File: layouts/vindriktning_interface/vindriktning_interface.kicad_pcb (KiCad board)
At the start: 2 copper layers, 8 parts

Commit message: Migrate layout partially
omit routing and zones amongst others
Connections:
- D1 pad 2: fan_controller-gnd-1 -> fan_controller-gnd
- FanConnector1 pad 1: fan_controller-gnd-1 -> fan_controller-gnd
- J1 pad 1: line -> line-2
- J1 pad 2: line-2 -> line-4
- Q1 pad 1: line-1 -> line-3
- Q1 pad 2: fan_controller-gnd-1 -> fan_controller-gnd
- Q1 pad 3: fan_controller-gnd -> fan_controller-gnd-1
- R1 pad 1: line-1 -> line-3
- R2 pad 2: fan_controller-gnd-1 -> fan_controller-gnd
- U1 pad 1: line-2 -> line-4
- U1 pad 4: line-3 -> line-1
- U1 pad 5: line-4 -> line
- U1 pad 8: line -> line-2
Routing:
- net fan_controller-gnd-1: track 6.53 -> 0.00 mm
- net fan_controller-gnd: track 0.00 -> 6.53 mm
- net line-3: track 0.00 -> 1.55 mm
- net line-1: track 1.55 -> 0.00 mm
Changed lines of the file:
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@@
     (net 1 "cathode")
     (net 2 "hv-1")
-    (net 3 "line")
+    (net 3 "line-2")
     (net 4 "fan_controller.fan_connector.footprint.pins[3].net-net")
-    (net 5 "line-1")
+    (net 5 "line-3")
     (net 6 "fan_controller-hv")
     (net 7 "fan_controller.fan_connector.footprint.pins[2].net-net")
@@
     (net 9 "hv")
     (net 10 "gnd")
-    (net 11 "fan_controller-gnd")
+    (net 11 "fan_controller-gnd-1")
     (net 12 "gnd-1")
-    (net 13 "line-4")
-    (net 14 "line-3")
+    (net 13 "line")
+    (net 14 "line-1")
     (net 15 "mount[0]")
-    (net 16 "fan_controller-gnd-1")
-    (net 17 "line-2")
+    (net 16 "fan_controller-gnd")
+    (net 17 "line-4")
     (footprint "atopile:R0603-ebcab9"
         (layer "F.Cu")
@@
             (layers "F.Cu" "F.Paste" "F.Mask")
             (remove_unused_layers no)
-            (net 5 "line-1"))
+            (net 5 "line-3"))
         (pad "2" smd rect
             (at 0.75 0 180)
@@
             (layers "F.Cu" "F.Paste" "F.Mask")
             (remove_unused_layers no)
-            (net 16 "fan_controller-gnd-1"))
+            (net 16 "fan_controller-gnd"))
         (pad "2" smd rect
             (at 0.63 -1.45 90)
@@
             (layers "F.Cu" "F.Paste" "F.Mask")
             (remove_unused_layers no)
-            (net 17 "line-2"))
+            (net 17 "line-4"))
         (pad "2" smd rect
             (at -0.25 1.55 180)
@@
             (layers "F.Cu" "F.Paste" "F.Mask")
             (remove_unused_layers no)
-            (net 14 "line-3"))
+            (net 14 "line-1"))
         (pad "5" smd rect
             (at 0.76 -1.55 180)
@@
             (layers "F.Cu" "F.Paste" "F.Mask")
             (remove_unused_layers no)
-            (net 13 "line-4"))
+            (net 13 "line"))
         (pad "6" smd rect
             (at 0.25 -1.55 180)
@@
             (layers "F.Cu" "F.Paste" "F.Mask")
             (remove_unused_layers no)
-            (net 3 "line")))
+            (net 3 "line-2")))
     (footprint "atopile:SOT-23-3_L2.9-W1.3-P1.90-LS2.4-BL-1-fcaf94"
         (layer "F.Cu")
@@
             (layers "F.Cu" "F.Paste" "F.Mask")
             (remove_unused_layers no)
-            (net 5 "line-1"))
+            (net 5 "line-3"))
         (pad "2" smd rect
             (at 0.95 1 0)
@@
             (layers "F.Cu" "F.Paste" "F.Mask")
             (remove_unused_layers no)
-            (net 16 "fan_controller-gnd-1"))
+            (net 16 "fan_controller-gnd"))
         (pad "3" smd rect
             (at 0 -1 0)
@@
             (layers "F.Cu" "F.Paste" "F.Mask")
             (remove_unused_layers no)
-            (net 11 "fan_controller-gnd")))
+            (net 11 "fan_controller-gnd-1")))
     (footprint "atopile:SOD-323_L1.8-W1.3-LS2.5-RD-b55baa"
         (layer "F.Cu")
@@
             (layers "F.Cu" "F.Paste" "F.Mask")
             (remove_unused_layers no)
-            (net 16 "fan_controller-gnd-1")))
+            (net 16 "fan_controller-gnd")))
     (footprint "atopile:CONN-SMD_ZH1.5-4AB-9aedad"
         (layer "F.Cu")
@@
             (layers "F.Cu" "F.Paste" "F.Mask")
             (remove_unused_layers no)
-            (net 3 "line"))
+            (net 3 "line-2"))
         (pad "2" smd rect
             (at -0.75 1.12 0)
@@
             (layers "F.Cu" "F.Paste" "F.Mask")
             (remove_unused_layers no)
-            (net 17 "line-2"))
+            (net 17 "line-4"))
         (pad "3" smd rect
             (at 0.75 1.12 0)
@@
             (layers "F.Cu" "F.Paste" "F.Mask")
             (remove_unused_layers no)
-            (net 16 "fan_controller-gnd-1")))
+            (net 16 "fan_controller-gnd")))
     (segment
         (start 10.75 -10.25)

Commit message: Regenerate layouts
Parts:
- moved U1 14.7 mm to (9.00, -13.5), turned to 90 degrees
- moved J1 13.4 mm to (10.0, -18.1)
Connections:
- J1 pad 1: line-2 -> line
- J1 pad 2: line-4 -> line-2
- J1 pad 3: hv -> hv-1
- J1 pad 4: gnd -> gnd-1
- Q1 pad 1: line-3 -> line-1
- R1 pad 1: line-3 -> line-1
- R1 pad 2: gnd-1 -> gnd
- U1 pad 1: line-4 -> line-2
- U1 pad 2: gnd -> gnd-1
- U1 pad 3: hv-1 -> hv
- U1 pad 4: line-1 -> line-4
- U1 pad 5: line -> line-3
- U1 pad 6: hv-1 -> hv
- U1 pad 7: hv -> hv-1
- U1 pad 8: line-2 -> line
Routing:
- net hv-1: track 0.00 -> 12.3 mm
- net line: track 0.00 -> 5.70 mm
- net line-2: track 0.00 -> 5.22 mm
- net hv: track 0.00 -> 3.14 mm, vias 0 -> 2
- net line-3: track 1.55 -> 0.00 mm
- net line-1: track 0.00 -> 1.55 mm

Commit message: Update layouts
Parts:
- D2: value infV -> (none)
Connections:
- J1 pad 1: line -> line-1
- J1 pad 4: gnd-1 -> gnd
- Q1 pad 1: line-1 -> line-3
- R1 pad 1: line-1 -> line-3
- R1 pad 2: gnd -> gnd-1
- U1 pad 2: gnd-1 -> gnd
- U1 pad 5: line-3 -> line
- U1 pad 8: line -> line-1
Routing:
- net line: track 5.70 -> 0.00 mm
- net line-1: track 1.55 -> 5.70 mm
- net line-3: track 0.00 -> 1.55 mm
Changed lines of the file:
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@@
     (net 1 "cathode")
     (net 2 "hv")
-    (net 3 "line")
+    (net 3 "line-1")
     (net 4 "fan_controller.fan_connector.footprint.pins[3].net-net")
-    (net 5 "line-1")
+    (net 5 "line-3")
     (net 6 "fan_controller-hv")
     (net 7 "fan_controller.fan_connector.footprint.pins[2].net-net")
     (net 8 "mount[1]")
     (net 9 "hv-1")
-    (net 10 "gnd-1")
+    (net 10 "gnd")
     (net 11 "fan_controller-gnd-1")
-    (net 12 "gnd")
-    (net 13 "line-3")
+    (net 12 "gnd-1")
+    (net 13 "line")
     (net 14 "line-4")
     (net 15 "mount[0]")
@@
             (layers "F.Cu" "F.Paste" "F.Mask")
             (remove_unused_layers no)
-            (net 5 "line-1"))
+            (net 5 "line-3"))
         (pad "2" smd rect
             (at 0.75 0 180)
@@
             (layers "F.Cu" "F.Paste" "F.Mask")
             (remove_unused_layers no)
-            (net 12 "gnd")))
+            (net 12 "gnd-1")))
     (footprint "atopile:CONN-SMD_1.25-2P-ea2134"
         (layer "F.Cu")
@@
             (layers "F.Cu" "F.Paste" "F.Mask")
             (remove_unused_layers no)
-            (net 10 "gnd-1"))
+            (net 10 "gnd"))
         (pad "3" smd rect
             (at 0.25 1.55 270)
@@
             (layers "F.Cu" "F.Paste" "F.Mask")
             (remove_unused_layers no)
-            (net 13 "line-3"))
+            (net 13 "line"))
         (pad "6" smd rect
             (at 0.25 -1.55 270)
@@
             (layers "F.Cu" "F.Paste" "F.Mask")
             (remove_unused_layers no)
-            (net 3 "line")))
+            (net 3 "line-1")))
     (footprint "atopile:SOT-23-3_L2.9-W1.3-P1.90-LS2.4-BL-1-fcaf94"
         (layer "F.Cu")
@@
             (layers "F.Cu" "F.Paste" "F.Mask")
             (remove_unused_layers no)
-            (net 5 "line-1"))
+            (net 5 "line-3"))
         (pad "2" smd rect
             (at 0.95 1 0)
@@
             (layers "F.Cu" "F.Paste" "F.Mask")
             (remove_unused_layers no)
-            (net 3 "line"))
+            (net 3 "line-1"))
         (pad "2" smd rect
             (at -0.75 1.12 0)
@@
             (layers "F.Cu" "F.Paste" "F.Mask")
             (remove_unused_layers no)
-            (net 10 "gnd-1"))
+            (net 10 "gnd"))
         (pad "5" smd rect
             (at -4.5 -1.12 0)
@@
                     (size 1 1)
                     (thickness 0.15))))
-        (property "Value" "infV"
+        (property "Value" ""
             (at 0 4 -90)
             (layer "F.Fab")

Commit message: Update layout
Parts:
- moved J1 18.9 mm to (11.1, 0.80), turned to 180 degrees
- moved D1 11.2 mm to (0.00, -3.50)
- moved D2 11.2 mm to (3.25, -3.25)
- moved FanConnector1 11.2 mm to (0.00, 0.00)
- moved Q1 11.2 mm to (-4.00, -4.50)
- moved R1 11.2 mm to (-3.75, -2.00)
- moved R2 11.2 mm to (0.00, -5.25)
- moved U1 10.6 mm to (6.50, -3.25), turned to 0 degrees
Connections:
- J1 pad 1: line-1 -> line
- J1 pad 2: line-2 -> line-1
- J1 pad 4: gnd -> gnd-1
- Q1 pad 1: line-3 -> line-4
- R1 pad 1: line-3 -> line-4
- R1 pad 2: gnd-1 -> gnd
- U1 pad 1: line-2 -> line-1
- U1 pad 2: gnd -> gnd-1
- U1 pad 4: line-4 -> line-3
- U1 pad 5: line -> line-2
- U1 pad 8: line-1 -> line
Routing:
- net line: track 0.00 -> 11.1 mm
- net line-2: track 5.22 -> 0.00 mm
- net line-1: track 5.70 -> 9.35 mm
- net hv-1: track 12.3 -> 15.7 mm, vias 0 -> 2
- net line-4: track 0.00 -> 1.55 mm
- net line-3: track 1.55 -> 1.20 mm, vias 0 -> 1

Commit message: do some layouts
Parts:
- removed D1: 450mV, atopile:SOD-323_L1.8-W1.3-LS2.5-RD-b55baa
- removed D2: , atopile:LED0805-R-RD-d1137b
- removed FanConnector1: , atopile:CONN-SMD_1.25-2P-ea2134
- removed J1: , atopile:CONN-SMD_ZH1.5-4AB-9aedad
- removed Q1: , atopile:SOT-23-3_L2.9-W1.3-P1.90-LS2.4-BL-1-fcaf94
- added C1: 100nF ±10% 50V X7R, atopile:C0603-bd72f6, F.Cu at (0.17, 11.2)
- added C2: 1µF ±10% 50V X5R, atopile:C0603-bd72f6, F.Cu at (-2.40, 8.30)
- added C3: 20pF ±5% 50V C0G, atopile:C0402-b3ef17, F.Cu at (8.54, 4.34)
- added C4: 20pF ±5% 50V C0G, atopile:C0402-b3ef17, F.Cu at (8.54, 6.64)
- added C5: 100nF ±10% 50V X7R, atopile:C0603-bd72f6, F.Cu at (-1.42, 11.2)
- added R3: 0Ω 100mW, atopile:R0603-ebcab9, F.Cu at (7.20, 2.50)
- added R4: 10kΩ ±1% 100mW, atopile:R0603-ebcab9, F.Cu at (-0.75, 8.20)
- added R5: 10kΩ ±1% 100mW, atopile:R0603-ebcab9, F.Cu at (6.60, -2.40)
- added R6: 10kΩ ±1% 100mW, atopile:R0603-ebcab9, F.Cu at (-3.00, 11.2)
- added S1: , atopile:KEY-SMD_4P-L4.2-W3.2-P2.20-LS4.6-a2ccf0, F.Cu at (4.17, 9.60)
- added S2: , atopile:KEY-SMD_4P-L4.2-W3.2-P2.20-LS4.6-a2ccf0, F.Cu at (-5.43, 9.60)
- added XTAL1: , atopile:CRYSTAL-SMD_L3.2-W1.5-1-214bf9, F.Cu at (6.90, 5.20)
- U1: footprint atopile:VSON8_L2.0-W2.3-P0.50-LS3.1-BL-9e6526 -> atopile:WIFIM-SMD_ESP32-C3-MINI-MINI-1U-1cb675
- moved R1 14.3 mm to (1.75, 11.2), turned to 90 degrees
- moved R2 13.5 mm to (1.60, 8.20), turned to -90 degrees
- moved U1 7.27 mm to (0.00, 0.00), turned to 90 degrees
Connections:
- net line-3 renamed mcu.esp32_c3_mini_1.ic.footprint.pins[33].net-net
- R1 pad 1: line-4 -> mcu.boot_switch-line
- R1 pad 2: gnd -> mcu-line
- R2 pad 1: cathode -> mcu-line
- R2 pad 2: fan_controller-gnd -> hv
- U1 pad 1: line-1 -> gnd
- U1 pad 2: gnd-1 -> gnd
- U1 pad 5: line-2 -> mcu-line-1
- U1 pad 6: hv -> mcu.esp32_c3_mini_1.ic-line
- U1 pad 7: hv-1 -> mcu.esp32_c3_mini_1.ic.footprint.pins[58].net-net
- U1 pad 8: line -> mcu-line
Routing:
- net mcu-line-2: track 0.00 -> 22.1 mm, vias 0 -> 2
- net hv-1: track 15.7 -> 0.00 mm, vias 2 -> 0
- net line: track 11.1 -> 0.00 mm
- net line-1: track 9.35 -> 0.00 mm
- net mcu-line: track 0.00 -> 7.37 mm
- net fan_controller-gnd: track 6.53 -> 0.00 mm
- net mcu.reset_switch-line: track 0.00 -> 5.64 mm
- net mcu.boot_switch-line: track 0.00 -> 5.63 mm
- net fan_controller-hv: track 5.20 -> 0.00 mm
- net mcu-line-7: track 0.00 -> 4.79 mm
- net hv: track 3.14 -> 7.66 mm, vias 2 -> 3
- net unnamed[0]: track 0.00 -> 3.84 mm
- net cathode: track 2.89 -> 0.00 mm
- net mcu-line-4: track 0.00 -> 2.21 mm
- net mcu-line-9: track 0.00 -> 1.67 mm
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- added copper zone on F.Cu, net gnd

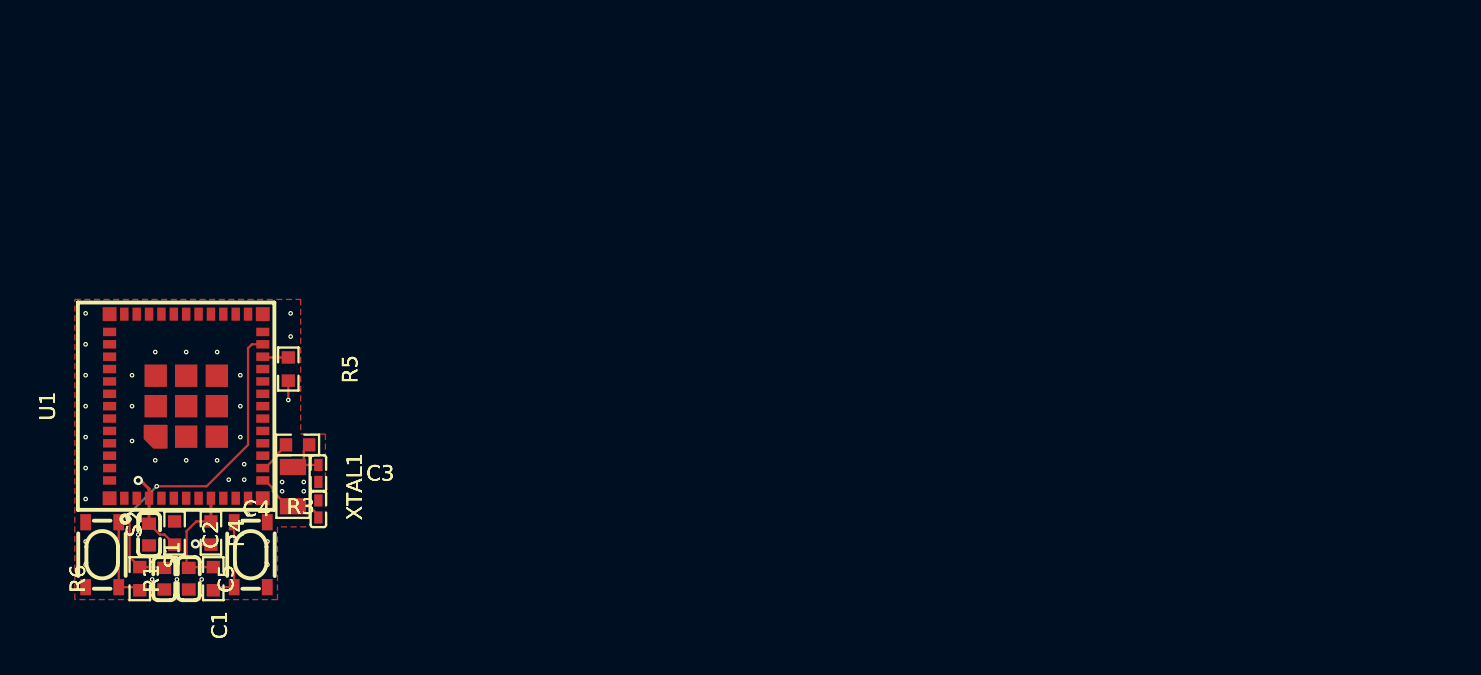
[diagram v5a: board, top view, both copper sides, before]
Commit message: Try to fix fuses
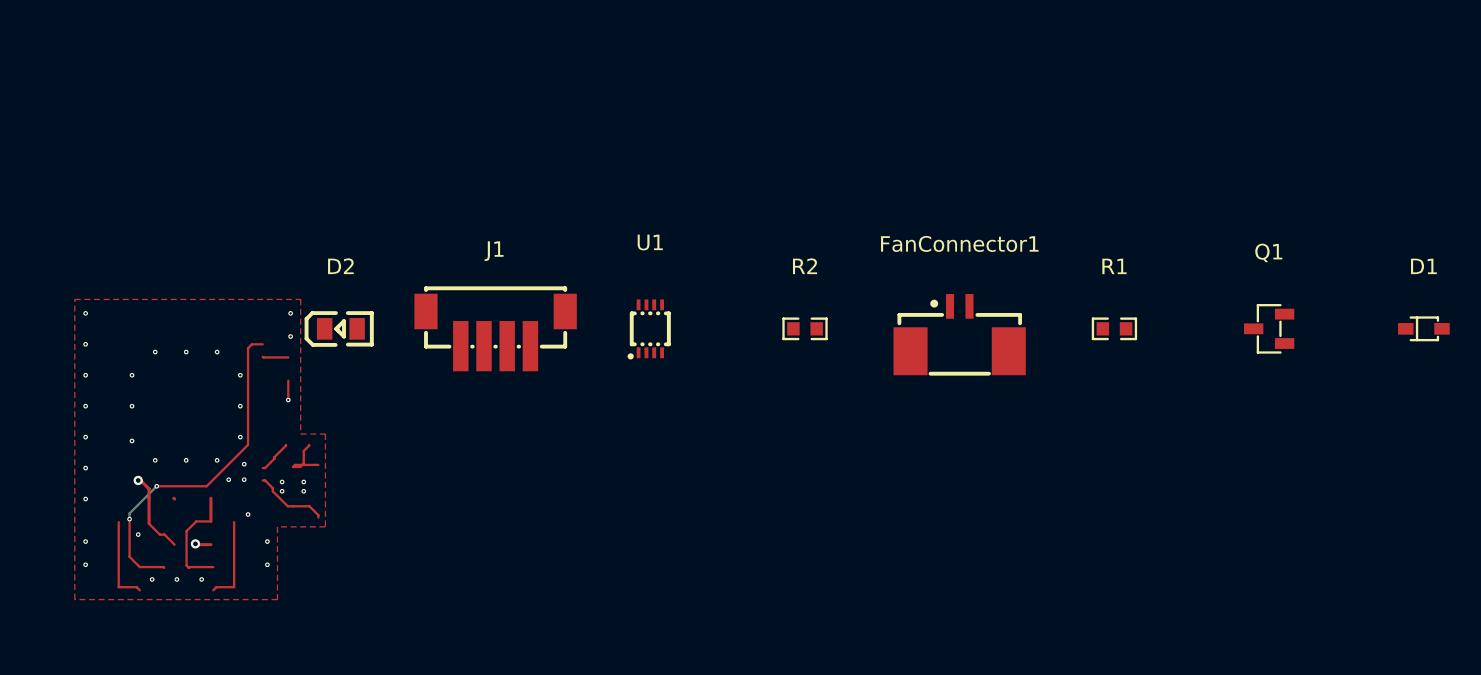
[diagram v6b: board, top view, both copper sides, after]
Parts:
- removed C1, C5: 100nF ±10% 50V X7R, atopile:C0603-bd72f6
- removed C2: 1µF ±10% 50V X5R, atopile:C0603-bd72f6
- removed C3, C4: 20pF ±5% 50V C0G, atopile:C0402-b3ef17
- removed R3: 0Ω 100mW, atopile:R0603-ebcab9
- removed R4, R5, R6: 10kΩ ±1% 100mW, atopile:R0603-ebcab9
- removed S1, S2: , atopile:KEY-SMD_4P-L4.2-W3.2-P2.20-LS4.6-a2ccf0
- removed XTAL1: , atopile:CRYSTAL-SMD_L3.2-W1.5-1-214bf9
- added D1: 450mV, atopile:SOD-323_L1.8-W1.3-LS2.5-RD-b55baa, F.Cu at (80.0, -5.00)
- added D2: , atopile:LED0805-R-RD-d1137b, F.Cu at (10.0, -5.00)
- added FanConnector1: , atopile:CONN-SMD_1.25-2P-ea2134, F.Cu at (50.0, -5.00)
- added J1: , atopile:CONN-SMD_ZH1.5-4AB-9aedad, F.Cu at (20.0, -5.00)
- added Q1: , atopile:SOT-23-3_L2.9-W1.3-P1.90-LS2.4-BR-688f29, F.Cu at (70.0, -5.00)
- U1: footprint atopile:WIFIM-SMD_ESP32-C3-MINI-MINI-1U-1cb675 -> atopile:VSON8_L2.0-W2.3-P0.50-LS3.1-BL-9e6526
- moved R1 60.4 mm to (60.0, -5.00), turned to 0 degrees
- moved R2 40.6 mm to (40.0, -5.00), turned to 0 degrees
- moved U1 30.4 mm to (30.0, -5.00), turned to 0 degrees
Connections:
- net mcu.esp32_c3_mini_1.ic.footprint.pins[33].net-net renamed line-4
- R1 pad 1: mcu.boot_switch-line -> line-2
- R1 pad 2: mcu-line -> gnd
- R2 pad 1: mcu-line -> cathode
- R2 pad 2: hv -> fan_controller-gnd
- U1 pad 1: gnd -> line
- U1 pad 2: gnd -> gnd-1
- U1 pad 3: hv -> hv-1
- U1 pad 5: mcu-line-1 -> line-3
- U1 pad 6: mcu.esp32_c3_mini_1.ic-line -> hv-1
- U1 pad 7: mcu.esp32_c3_mini_1.ic.footprint.pins[58].net-net -> hv
- U1 pad 8: mcu-line -> line-1
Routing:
- net (no net): track 0.00 -> 61.0 mm, vias 0 -> 42
- net mcu-line-2: track 22.1 -> 0.00 mm, vias 2 -> 0
- net hv: track 7.66 -> 0.00 mm, vias 3 -> 0
- net mcu-line: track 7.37 -> 0.00 mm
- net mcu.reset_switch-line: track 5.64 -> 0.00 mm
- net mcu.boot_switch-line: track 5.63 -> 0.00 mm
- net mcu-line-7: track 4.79 -> 0.00 mm
- net unnamed[0]: track 3.84 -> 0.00 mm
- net mcu-line-4: track 2.21 -> 0.00 mm
- net mcu-line-9: track 1.67 -> 0.00 mm
- net gnd: vias 37 -> 0
- added copper zone on F.Cu, net (none)
- removed copper zone on F.Cu, net gnd
